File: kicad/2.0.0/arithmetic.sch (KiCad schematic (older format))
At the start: 31 parts

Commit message: added power leds and test points to 2.0.0
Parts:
- removed J?: POWER, TerminalBlock_TE-Connectivity:TerminalBlock_TE_282834-3_1x03_P2.54mm_Horizontal, symbol Connector:Screw_Terminal_01x03
- removed J?: DIFFX, Connector_SMA:SMA_Molex_73251-2120_EdgeMount, symbol Connector:Conn_Coaxial
- removed J?: DIFFY, Connector_SMA:SMA_Molex_73251-2120_EdgeMount, symbol Connector:Conn_Coaxial
- removed J?: SUM, Connector_SMA:SMA_Molex_73251-2120_EdgeMount, symbol Connector:Conn_Coaxial
- added C? (x2): 100n, Capacitor_SMD:C_0603_1608Metric, symbol Device:C_Small
- added C? (x2): 10u, Capacitor_SMD:C_1206_3216Metric, symbol Device:C_Small
- added C? (x2): 1u, Capacitor_SMD:C_0603_1608Metric, symbol Device:C_Small
- added D? (x4): D_Small, symbol Device:D_Small
- added D? (x2): LED, symbol Device:LED
- added R? (x2): 120, Resistor_SMD:R_0603_1608Metric, symbol Device:R_Small
- added R? (x2): 1.1k, Resistor_SMD:R_0603_1608Metric, symbol Device:R_Small
- added R?: 510, symbol Device:R_Small
- added R?: 470, symbol Device:R_Small
- added TP?: -15V, symbol Connector:TestPoint
- added TP? (x4): +12V, symbol Connector:TestPoint
- added TP? (x2): -12V, symbol Connector:TestPoint
- added TP?: DIFFX, symbol Connector:TestPoint
- added TP?: DIFFY, symbol Connector:TestPoint
- added TP?: SUM, symbol Connector:TestPoint
- added TP?: SUM-, symbol Connector:TestPoint
- added TP?: SUM+, symbol Connector:TestPoint
- added TP?: DIFFX-, symbol Connector:TestPoint
- added TP?: DIFFY-, symbol Connector:TestPoint
- added TP?: DIFFX+, symbol Connector:TestPoint
- added TP?: DIFFY+, symbol Connector:TestPoint
- added TP?: +15V, symbol Connector:TestPoint
- added TP?: GND, symbol Connector:TestPoint
- added U?: LM337, Package_TO_SOT_SMD:SOT-223-3_TabPin2, symbol Regulator_Linear:LM337_SOT223
- added U?: LM317, Package_TO_SOT_SMD:SOT-223-3_TabPin2, symbol Regulator_Linear:LM317_3PinPackage
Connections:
- wire segments 95 -> 170
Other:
- note added: "Basic circuit adopted from the ‘Typical applications’ section in the LM337-N datasheet.\nAdded flyback and reverse polarization diodes for protection."
- note added: "Forward voltages for LEDs:\nRed Vf = 1.8 V, Blue Vf = 3.1 V"
- note added: "POWER INPUT"
- note added: "POWER LEDS"
- note added: "R = (Vs - Vf) / I"
- note added: "SIGNAL OUTPUT"
- note added: "VOLTAGE REGULATORS"
- note added: "Vout = 1.25 V * (1 + R / 120) = 12.7 V"
- note removed: "OUTPUT CONNECTORS"
- note removed: "POWER CONNECTOR"
- moved on the sheet: C?, R?

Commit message: changed arithmetic resistors to 10k, added caps to arithmetic op amps
The increase in resistor values is motivated to avoid heat or power
throttle of the op amps.
The feedback caps on the arithmetic increases stability.
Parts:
- removed C?: 100n, Capacitor_SMD:C_0603_1608Metric, symbol Device:C_Small
- removed R? (x7): 1k, Resistor_SMD:R_0603_1608Metric, symbol Device:R_Small
- removed TP?: DIFFX, symbol Connector:TestPoint
- removed TP?: DIFFY, symbol Connector:TestPoint
- removed TP?: SUM, symbol Connector:TestPoint
- removed TP?: SUM-, symbol Connector:TestPoint
- removed TP?: DIFFX-, symbol Connector:TestPoint
- removed TP?: DIFFY-, symbol Connector:TestPoint
- removed TP?: DIFFX+, symbol Connector:TestPoint
- removed TP?: DIFFY+, symbol Connector:TestPoint
- removed U? (x3): OPA2197IDR, Package_SO:SOIC-8_3.9x4.9mm_P1.27mm, symbol Amplifier_Operational:OPA2197IDR
- removed U? (x2): OPA197IDR, Package_SO:SOIC-8_3.9x4.9mm_P1.27mm, symbol Amplifier_Operational:OPA197IDR
- added C? (x6): 5p, symbol Device:C_Small
- added C?: 100n, Capacitor_SMD:C_0603_1608Metric, symbol Device:C_Small
- added R? (x7): 10k, Resistor_SMD:R_0603_1608Metric, symbol Device:R_Small
- added TP?: SUM, symbol Connector:TestPoint
- added TP?: DIFFX, symbol Connector:TestPoint
- added TP?: SUM-, symbol Connector:TestPoint
- added TP?: DIFFX+, symbol Connector:TestPoint
- added TP?: DIFFX-, symbol Connector:TestPoint
- added TP?: DIFFY, symbol Connector:TestPoint
- added TP?: DIFFY+, symbol Connector:TestPoint
- added TP?: DIFFY-, symbol Connector:TestPoint
- added U? (x3): OPA2197xD, Package_SO:SOIC-8_3.9x4.9mm_P1.27mm, symbol Amplifier_Operational:OPA2197xD
- added U?: OPA197xDBV, Package_TO_SOT_SMD:SOT-23-5, symbol Amplifier_Operational:OPA197xDBV
- R? (x11): value 1k -> 10k
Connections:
- wire segments 170 -> 192
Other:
- note added: "DIFFX = (X2 + Y1) - (X1 + Y2)"
- note added: "DIFFY = (X2 + Y2) - (X1 + Y1)"
- note removed: "DIFFX = (X2 + Y1) - (X1 + Y2)\nDIFFY = (X2 + Y2) - (X1 + Y1)"
- moved on the sheet: C?, R?, TP?

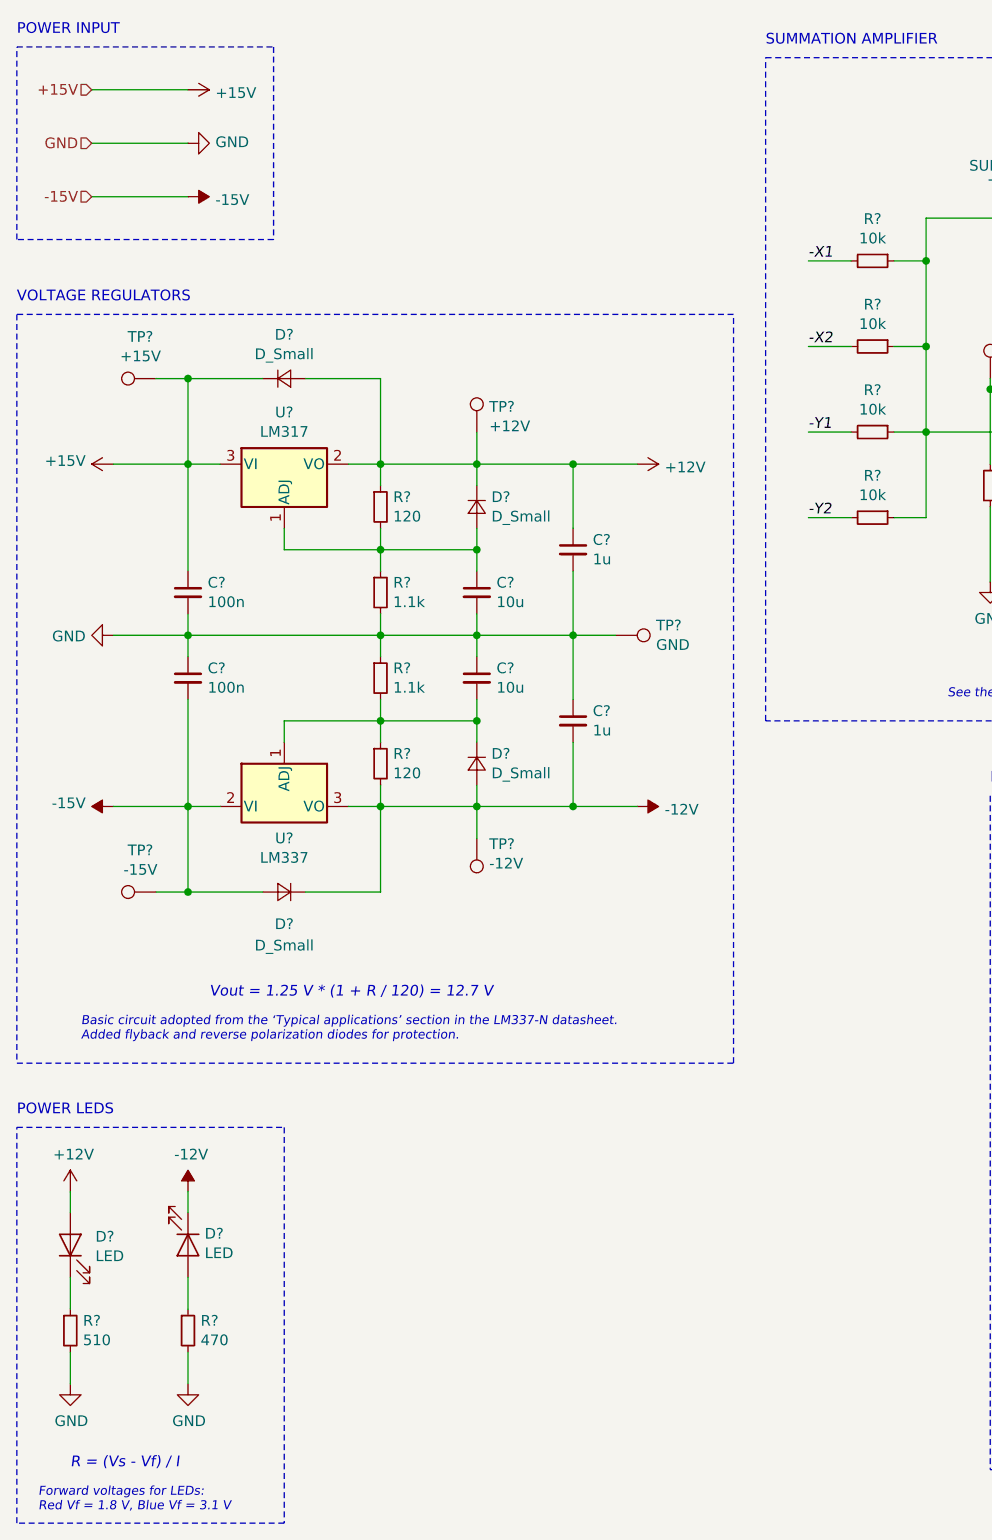
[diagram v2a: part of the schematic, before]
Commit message: replaced OPAx197s with standard library symbols, increased voltage regulator caps
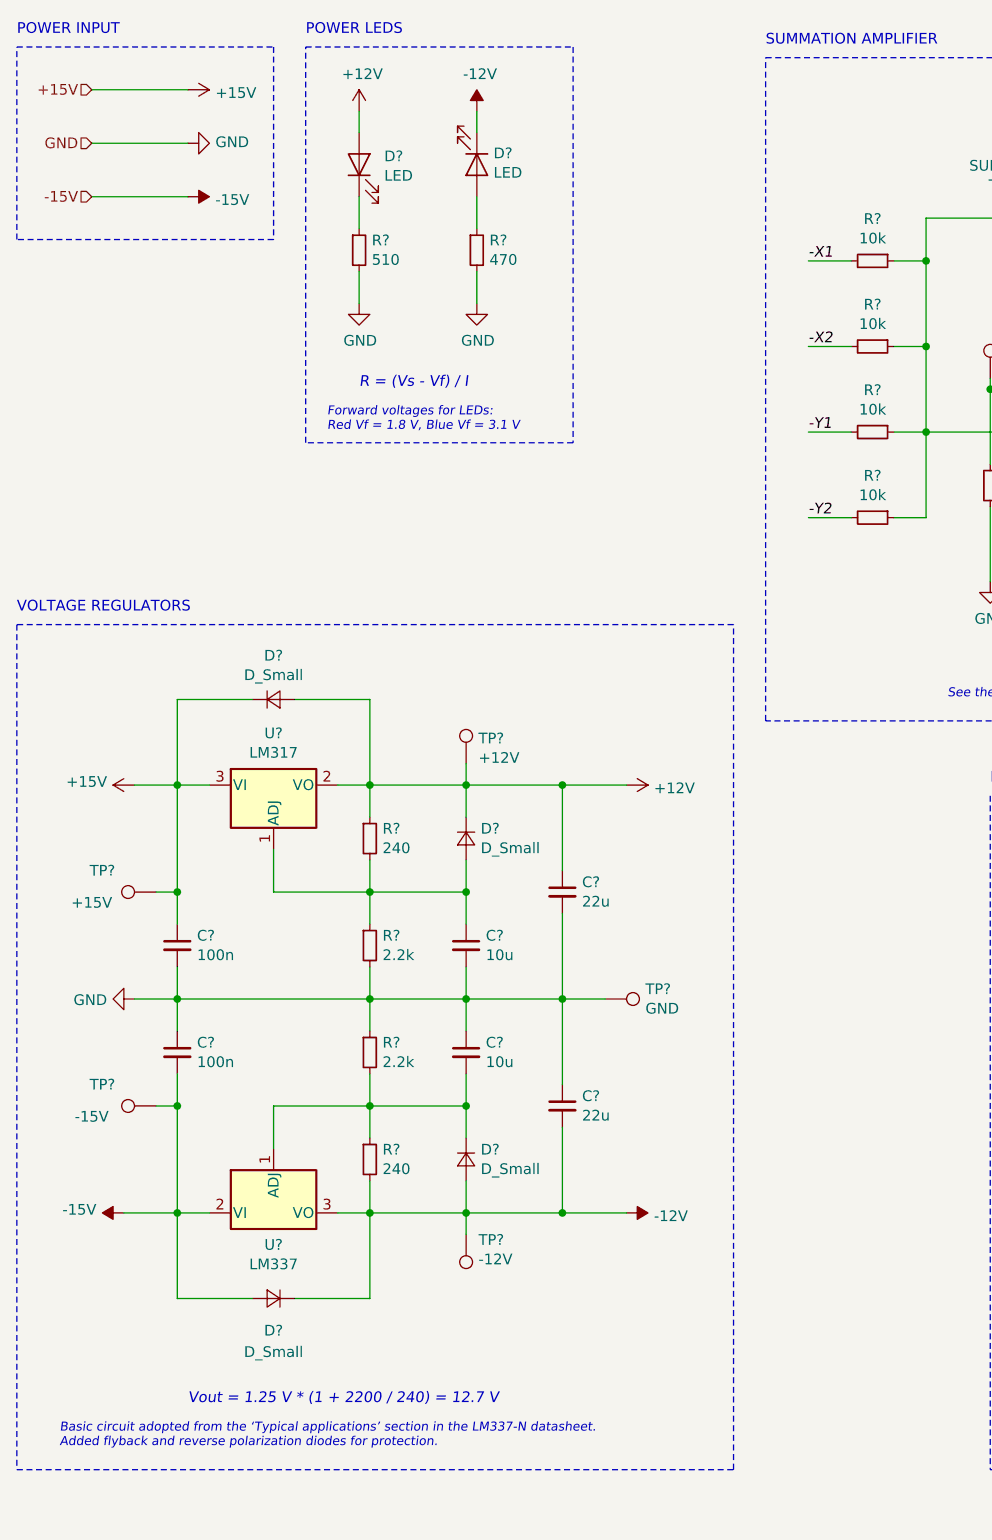
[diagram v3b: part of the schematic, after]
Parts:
- C? (x2): value 1u -> 22u
- R? (x2): value 120 -> 240
- R? (x2): value 1.1k -> 2.2k
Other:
- note added: "Vout = 1.25 V * (1 + 2200 / 240) = 12.7 V"
- note removed: "Vout = 1.25 V * (1 + R / 120) = 12.7 V"
- moved on the sheet: C?, D?, R?, TP?, U?

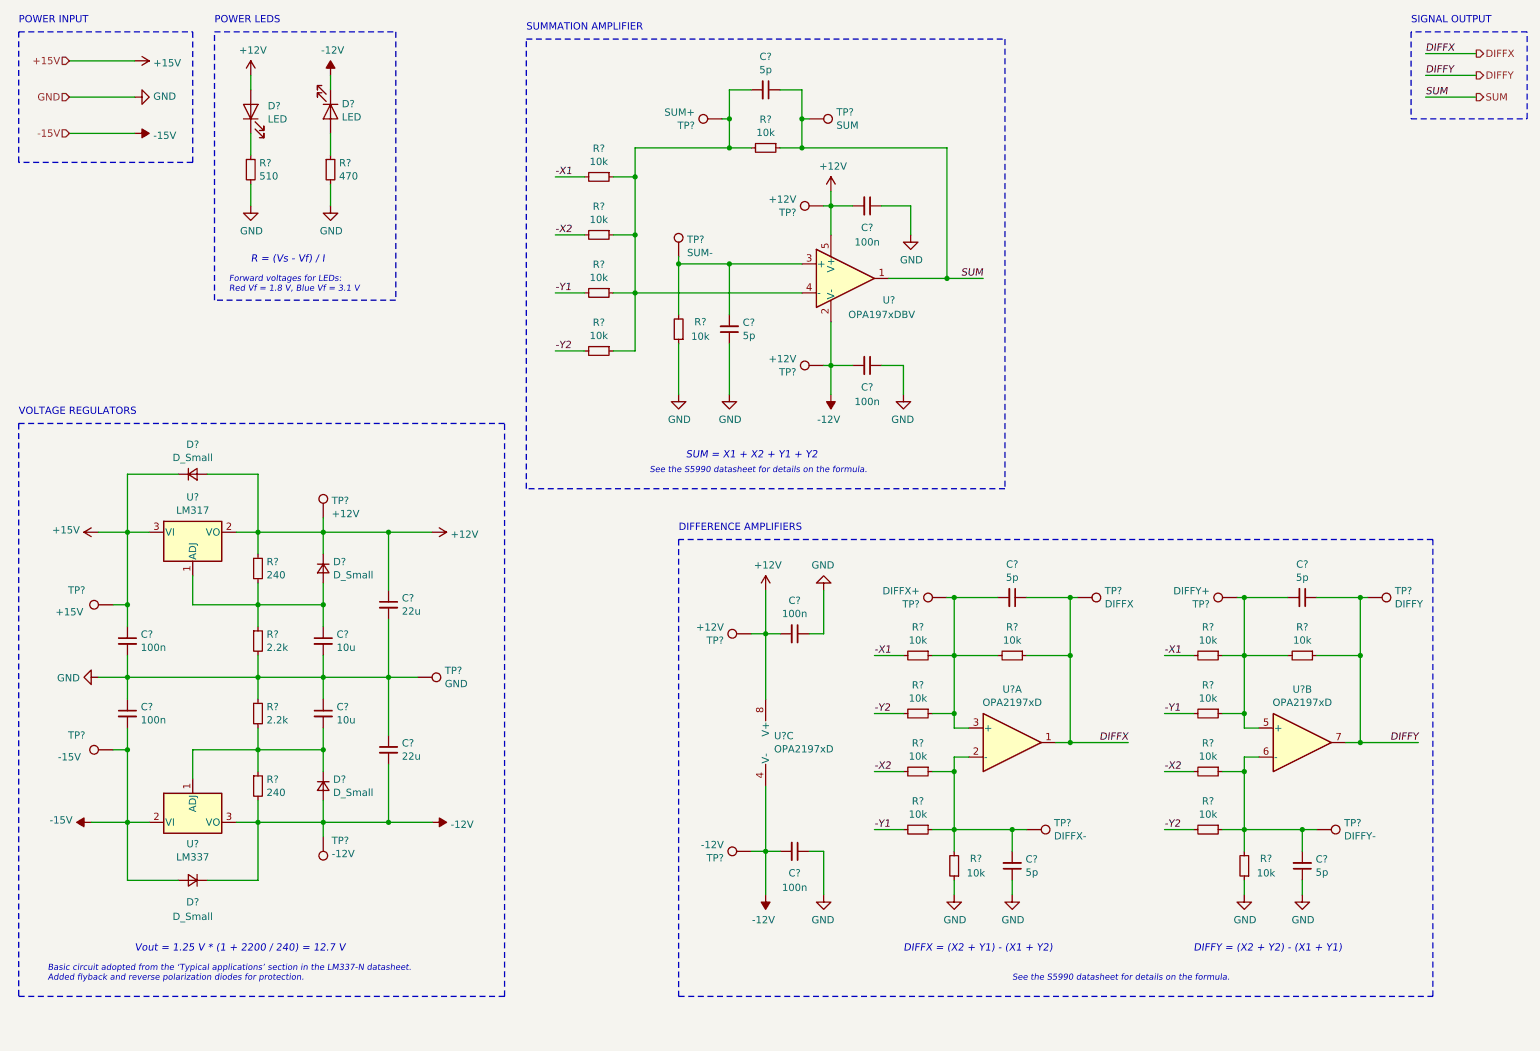
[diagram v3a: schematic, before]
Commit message: created extra projects for arithmetic and detector sheet
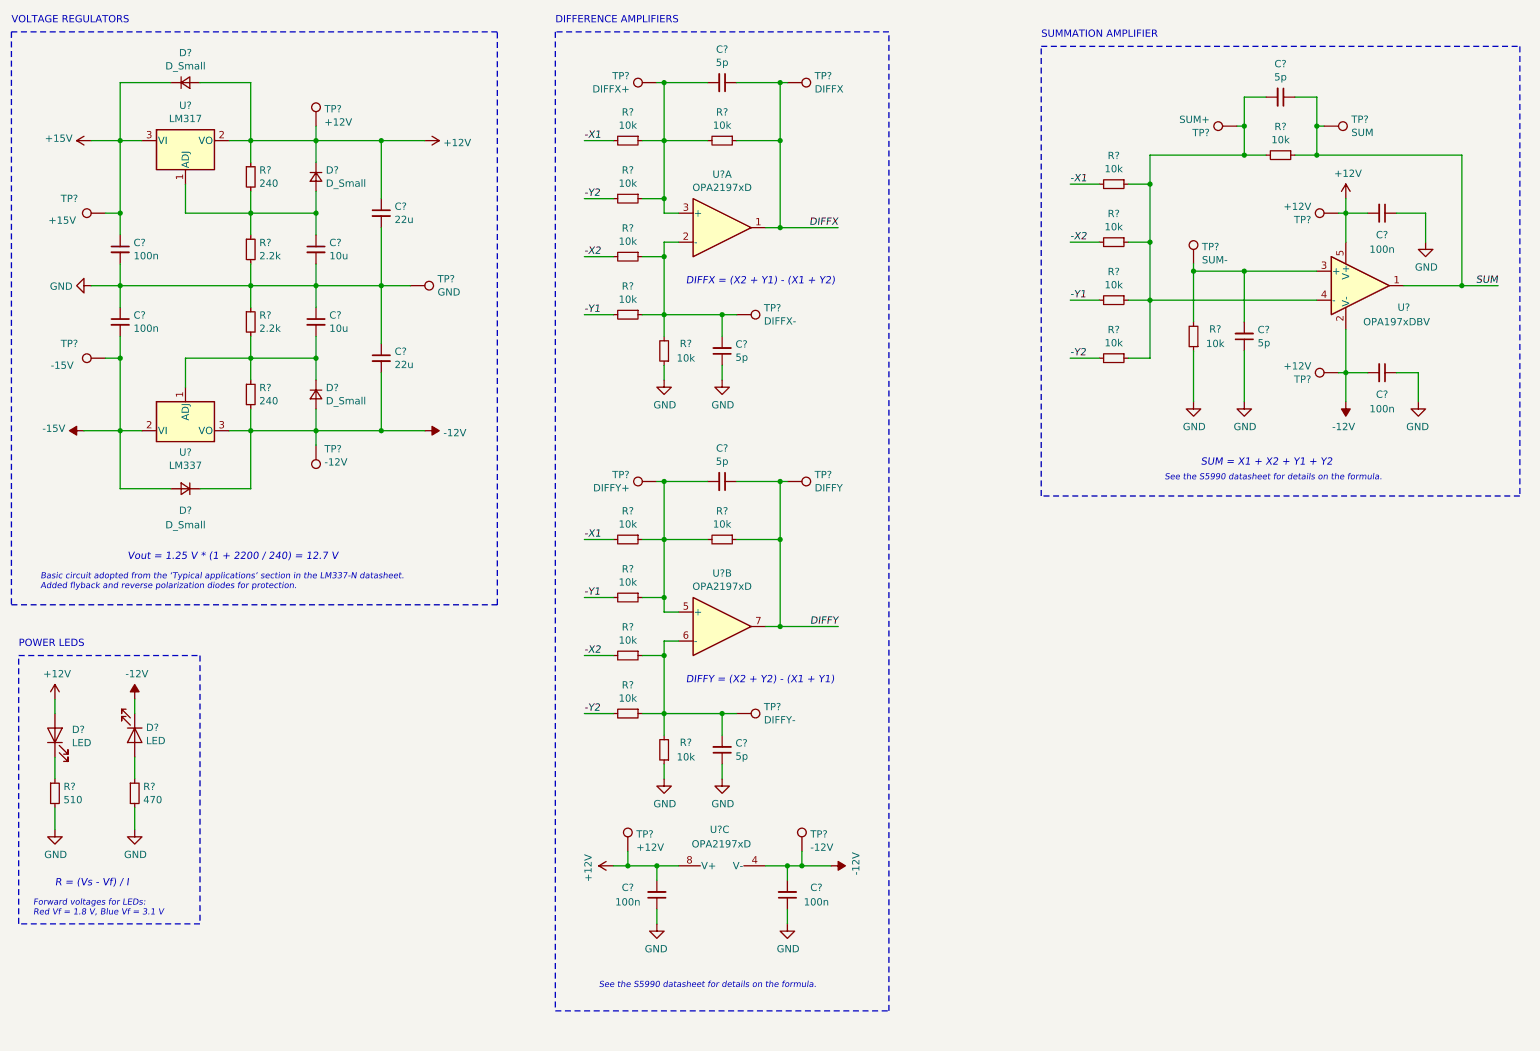
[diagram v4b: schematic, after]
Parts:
- removed TP?: +12V, symbol Connector:TestPoint
- removed TP?: -12V, symbol Connector:TestPoint
- removed TP?: DIFFX+, symbol Connector:TestPoint
- removed TP?: DIFFY+, symbol Connector:TestPoint
- added TP?: DIFFY+, symbol Connector:TestPoint
- added TP?: DIFFX+, symbol Connector:TestPoint
- added TP?: +12V, symbol Connector:TestPoint
- added TP?: -12V, symbol Connector:TestPoint
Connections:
- net +12V: now also TP?.1
- net -12V: now also TP?.1
- net at C?.2, R?.1, R?.1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: now also TP?.1 (x2)
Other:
- note removed: "POWER INPUT"
- note removed: "SIGNAL OUTPUT"
- moved on the sheet: C?, D?, R?, TP?, U?, U?A, U?B, U?C
